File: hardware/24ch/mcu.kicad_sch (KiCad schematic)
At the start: 21 parts, among them J501 AVR ISP, J502 LCD 20x4 HEADER, SW501 UP, SW502 DOWN, SW503 SET, SW504 ESC, SW505 ACK, U501 ATmega1284P-AU, Y501 8MHz

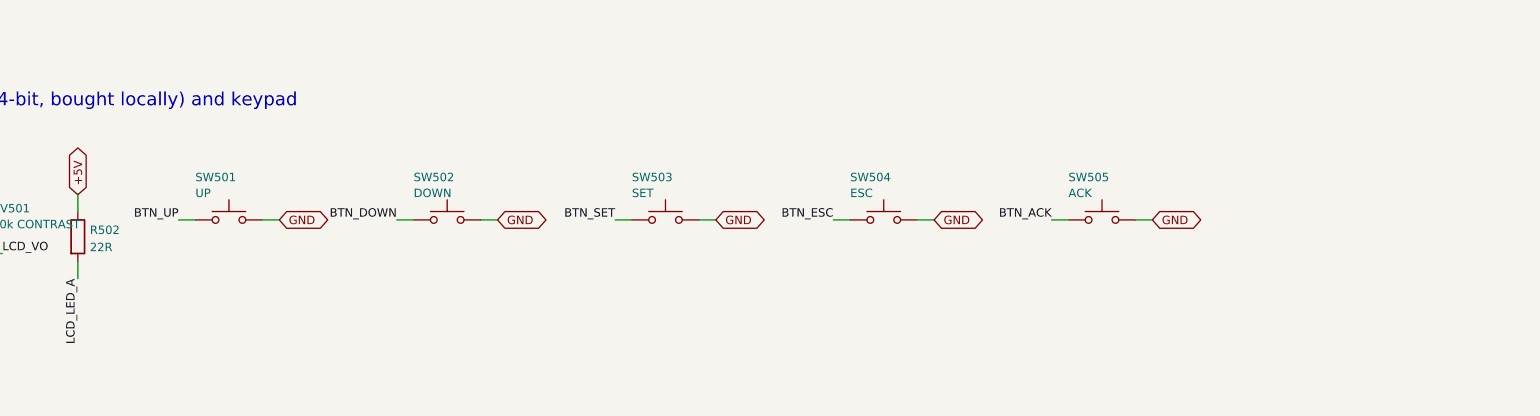
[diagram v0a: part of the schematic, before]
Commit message: 24ch board: I-111 cap repairs (0035), crystal (I-121), J503 panel header, fiducials, silk, V_BIAS guard (I-105)
Co-Authored-By: Claude Opus 5.5 <noreply@anthropic.com>
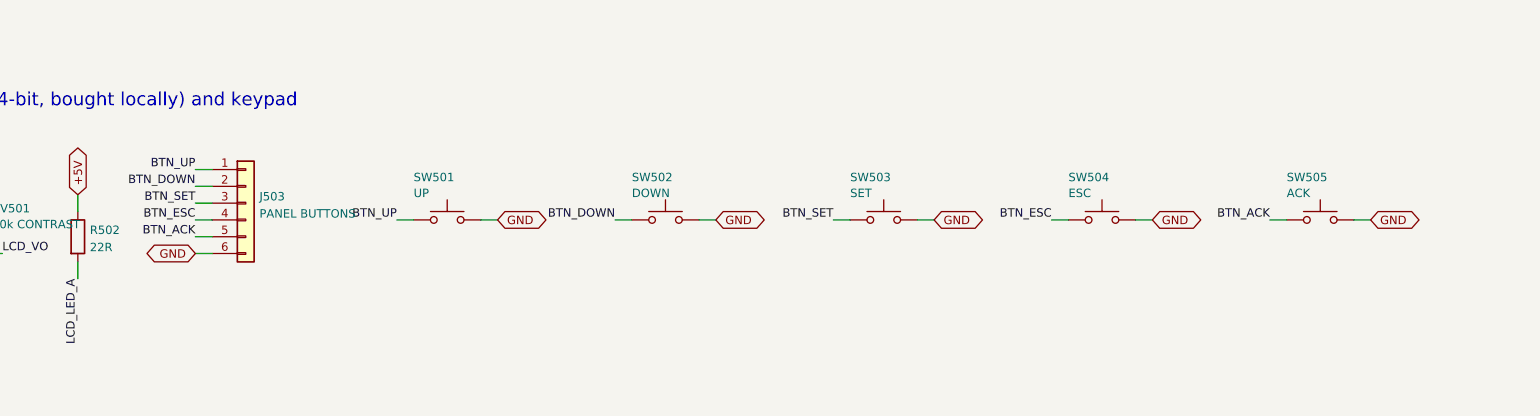
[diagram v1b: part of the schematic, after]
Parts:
- added J503: PANEL BUTTONS, Connector_JST:JST_XH_B6B-XH-A_1x06_P2.50mm_Vertical, symbol Connector_Generic:Conn_01x06
- SW501, SW502, SW503, SW504, SW505: LCSC (none) -> C7470135; MPN (none) -> ZX-QC66-9.5CJ; Manufacturer (none) -> Megastar
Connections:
- net BTN_ACK: now also J503.5 (Pin_5)
- net BTN_DOWN: now also J503.2 (Pin_2)
- net BTN_ESC: now also J503.4 (Pin_4)
- net BTN_SET: now also J503.3 (Pin_3)
- net BTN_UP: now also J503.1 (Pin_1)
- net GND: now also J503.6 (Pin_6)
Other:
- moved on the sheet: SW501, SW502, SW503, SW504, SW505

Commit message: 24ch cheaper-parts variant (0036): TMP126, CA-IS3761HW, RS-485 DNP, drop-in swaps
- CJ sensors ADT7310 x6 -> TMP126DCKR (C5219998); R443 22k DIN_ISO-DOUT_ISO for the
  3-wire SIO, R415 removed, ALERT grounded. Sensors moved <= 8 mm to clear spots beside
  their 100 nF (no closer spot to the terminals without touching TC traces, 0035 D2).
- ISO7761 -> CA-IS3761HW (same pinout, 5F/1R, default high); BOCHEN 3296W trimmer;
  SAMWHA 22u 1210.
- RS-485 block DNP: footprints kept; fab.py drops DNP parts from BOM/CPL and writes
  DNP.txt; cost.py skips them. External window watchdog tried and removed (owner).
- gen/delta.py: carry a schematic change onto the routed board (replace/add/remove,
  re-net, DNP, OLD>NEW@DEG reuse); it never deletes another net's track under a pad.
- Board: incremental edits only; analog nets (TC*, V_BIAS, VREF, REF*) identical to
  the pre-0036 board. Gates: ERC 0/0 (471 symbols); fab.py DRC/unconnected/parity
  0/0/0; pincaps 0 over. Parts ~$105 -> ~$72/board (CALCULATIONS 8.1, by hand).
- Docs: decision 0036, CALCULATIONS 8, ISSUES (I-109, I-114, I-119, I-104, I-094,
  new I-123 stock), STATE, 24ch README, superseded.txt.

Co-Authored-By: Claude Opus 5.5 <noreply@anthropic.com>
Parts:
- RV501: LCSC C34846 -> C118954; MPN 3296W-1-103LF -> 3296W-1-103; Manufacturer Bourns -> BOCHEN
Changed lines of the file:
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@@
 			)
 		)
-		(property "Description" "outside the LCD shadow"
+		(property "Description" "outside the LCD shadow; 3296W outline (0036)"
 			(at 53.34 180.34 0)
 			(effects
@@
 			)
 		)
-		(property "MPN" "3296W-1-103LF"
+		(property "MPN" "3296W-1-103"
 			(at 53.34 180.34 0)
 			(effects
@@
 			)
 		)
-		(property "Manufacturer" "Bourns"
+		(property "Manufacturer" "BOCHEN"
 			(at 53.34 180.34 0)
 			(effects
@@
 			)
 		)
-		(property "LCSC" "C34846"
+		(property "LCSC" "C118954"
 			(at 53.34 180.34 0)
 			(effects

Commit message: 24ch REV A4 (WIP): gated TMP126 SIO driver, PD5 = SIO_WR_N, ESC via diodes
- PD5 (was BTN_ESC) drives SIO_WR_N through spare U405 channel C to U411
  74LVC1G125 (OE); DIN -> U411 -> R446 220R -> DOUT_ISO; R445 10k, R447 100k,
  C421 100n, R439 10k pull-up. R443 22k removed (R446 reuses its footprint).
  Same circuit as hardware/family (fixes the TMP126 SIO edge, 1.2-1.6 us vs 100 ns).
- ESC button kept: D501/D502 1N4148W pull BTN_UP and BTN_DOWN together;
  firmware reads UP+DOWN as ESC.
- Board edited incrementally (delta.py, capnear.py, maze.py with In2 for
  SIO_DRV / SIO_WR_N_ISO); dead DIN branch to the old R443 pad removed.
- Gates: build.py ERC 0 errors 0 warnings, netlist 0 mismatches;
  finish.py DRC (errors, refilled) 0 violations, 0 unconnected; pincaps 0 over
  (U411 added). Silk, full DRC, fab release still to do.
- Title/release names REV A4.

Co-Authored-By: Claude Opus 5.5 <noreply@anthropic.com>
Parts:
- added D501, D502: 1N4148W, Diode_SMD:D_SOD-123, symbol Device:D
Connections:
- net BTN_DOWN: now also D502.2 (A)
- net BTN_ESC: now also D501.1 (K), D502.1 (K); no longer U501.14 (PD5)
- net BTN_UP: now also D501.2 (A)
- new net SIO_WR_N: U501.14 (PD5)
